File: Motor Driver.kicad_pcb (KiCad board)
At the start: 2 copper layers, 42 parts, among them CON1 AVR-ISP-6, J1 Conn_01x02, J10 Conn_01x04, J3 Conn_01x06, J5 Conn_01x04, J7 Conn_01x02, J8 Conn_01x02, J9 Conn_01x03, Q1 IRF3205, Q2 IRF3205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

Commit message: Minor Changes
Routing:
- net Net-(R5-Pad2): track 5.14 -> 5.92 mm
- net /IN2: track 65.6 -> 66.3 mm
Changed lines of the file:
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@@
     (thickness 1.6)
     (drawings 0)
-    (tracks 348)
+    (tracks 346)
     (zones 0)
     (modules 42)
@@
   (segment (start 133.477 130.135) (end 136.946 130.135) (width 0.6) (layer B.Cu) (net 2))
   (segment (start 136.946 130.135) (end 136.9695 130.1115) (width 0.6) (layer B.Cu) (net 2))
+  (segment (start 79.547318 94.214528) (end 79.547318 92.941736) (width 2) (layer B.Cu) (net 3))
+  (segment (start 79.547318 92.941736) (end 79.5655 92.923554) (width 2) (layer B.Cu) (net 3))
+  (segment (start 79.5655 92.923554) (end 79.5655 91.5035) (width 2) (layer B.Cu) (net 3))
+  (segment (start 94.361 88.773) (end 101.75494 96.16694) (width 2) (layer B.Cu) (net 3))
+  (segment (start 79.5655 91.5035) (end 82.296 88.773) (width 2) (layer B.Cu) (net 3))
+  (segment (start 82.296 88.773) (end 94.361 88.773) (width 2) (layer B.Cu) (net 3))
+  (segment (start 101.75494 96.16694) (end 101.75494 102.4636) (width 2) (layer B.Cu) (net 3))
   (segment (start 107.11688 151.257) (end 107.11688 152.00757) (width 2) (layer B.Cu) (net 3))
   (segment (start 107.11688 152.00757) (end 104.11739 155.00706) (width 2) (layer B.Cu) (net 3))
@@
   (via (at 104.894742 132.490462) (size 1.8) (drill 0.8) (layers F.Cu B.Cu) (net 3))
   (segment (start 107.609 140.421937) (end 106.938063 139.751) (width 2) (layer B.Cu) (net 3))
-  (segment (start 79.547318 94.214528) (end 79.547318 92.941736) (width 2) (layer B.Cu) (net 3))
-  (segment (start 79.547318 92.941736) (end 79.5655 92.923554) (width 2) (layer B.Cu) (net 3))
-  (segment (start 79.5655 92.923554) (end 79.5655 91.5035) (width 2) (layer B.Cu) (net 3))
-  (segment (start 79.5655 91.5035) (end 82.296 88.773) (width 2) (layer B.Cu) (net 3))
-  (segment (start 101.75494 98.71354) (end 101.75494 102.4636) (width 2) (layer B.Cu) (net 3))
-  (segment (start 82.296 88.773) (end 94.361 88.773) (width 2) (layer B.Cu) (net 3))
-  (segment (start 94.361 88.773) (end 95.9485 90.3605) (width 2) (layer B.Cu) (net 3))
-  (segment (start 95.9485 90.3605) (end 95.9485 92.9071) (width 2) (layer B.Cu) (net 3))
-  (segment (start 95.9485 92.9071) (end 101.75494 98.71354) (width 2) (layer B.Cu) (net 3))
   (via (at 94.234 132.461) (size 1.8) (drill 0.8) (layers F.Cu B.Cu) (net 3))
   (segment (start 88.011 132.461) (end 94.234 132.461) (width 0.6) (layer B.Cu) (net 3))
@@
   (segment (start 79.502 143.796) (end 79.502 140.083001) (width 0.6) (layer B.Cu) (net 5))
   (segment (start 79.502 140.083001) (end 79.582 140.003001) (width 0.6) (layer B.Cu) (net 5))
-  (segment (start 85.516318 107.422528) (end 78.702818 107.422528) (width 0.6) (layer B.Cu) (net 6))
-  (segment (start 78.702818 107.422528) (end 76.454 109.671346) (width 0.6) (layer B.Cu) (net 6))
-  (segment (start 76.454 109.671346) (end 76.454 112.75071) (width 0.6) (layer B.Cu) (net 6))
-  (segment (start 76.454 112.75071) (end 76.586818 112.883528) (width 0.6) (layer B.Cu) (net 6))
-  (segment (start 76.586818 112.883528) (end 78.086818 112.883528) (width 0.6) (layer B.Cu) (net 6))
-  (segment (start 77.510531 112.307241) (end 78.086818 112.883528) (width 0.6) (layer B.Cu) (net 6))
+  (segment (start 85.516318 107.422528) (end 77.980629 107.422528) (width 0.6) (layer B.Cu) (net 6))
+  (segment (start 77.980629 107.422528) (end 75.699332 109.703825) (width 0.6) (layer B.Cu) (net 6))
+  (segment (start 75.699332 109.703825) (end 75.699332 112.222694) (width 0.6) (layer B.Cu) (net 6))
+  (segment (start 75.699332 112.222694) (end 76.360166 112.883528) (width 0.6) (layer B.Cu) (net 6))
+  (segment (start 76.360166 112.883528) (end 78.086818 112.883528) (width 0.6) (layer B.Cu) (net 6))
   (segment (start 81.647318 112.892527) (end 78.095817 112.892527) (width 0.6) (layer B.Cu) (net 6))
   (segment (start 78.095817 112.892527) (end 78.086818 112.883528) (width 0.6) (layer B.Cu) (net 6))
+  (segment (start 84.754318 98.151528) (end 84.754318 99.880295) (width 0.6) (layer B.Cu) (net 7))
+  (segment (start 84.754318 99.880295) (end 88.714948 103.840925) (width 0.6) (layer B.Cu) (net 7))
+  (segment (start 88.714948 103.840925) (end 88.714948 107.731748) (width 0.6) (layer B.Cu) (net 7))
+  (segment (start 88.714948 107.731748) (end 87.024168 109.422528) (width 0.6) (layer B.Cu) (net 7))
+  (segment (start 87.024168 109.422528) (end 85.516318 109.422528) (width 0.6) (layer B.Cu) (net 7))
   (segment (start 82.087318 94.214528) (end 82.087318 93.178339) (width 2) (layer B.Cu) (net 7))
   (segment (start 82.087318 93.178339) (end 83.710356 91.555301) (width 2) (layer B.Cu) (net 7))
@@
   (segment (start 89.274768 91.555301) (end 90.215318 92.495851) (width 2) (layer B.Cu) (net 7))
   (segment (start 90.215318 92.495851) (end 90.215318 94.214528) (width 2) (layer B.Cu) (net 7))
-  (segment (start 84.754318 98.151528) (end 84.754318 100.382752) (width 0.6) (layer B.Cu) (net 7))
-  (segment (start 84.754318 100.382752) (end 88.30904 103.937474) (width 0.6) (layer B.Cu) (net 7))
-  (segment (start 88.30904 103.937474) (end 88.30904 108.137656) (width 0.6) (layer B.Cu) (net 7))
-  (segment (start 88.30904 108.137656) (end 87.024168 109.422528) (width 0.6) (layer B.Cu) (net 7))
-  (segment (start 87.024168 109.422528) (end 85.516318 109.422528) (width 0.6) (layer B.Cu) (net 7))
   (segment (start 58.801 122.61088) (end 59.55157 122.61088) (width 2) (layer B.Cu) (net 7))
   (segment (start 59.55157 122.61088) (end 76.839701 105.322749) (width 2) (layer B.Cu) (net 7))
@@
   (segment (start 86.786318 123.932528) (end 86.786318 120.571527) (width 0.6) (layer B.Cu) (net 26))
   (segment (start 86.786318 120.571527) (end 86.727318 120.512527) (width 0.6) (layer B.Cu) (net 26))
-  (segment (start 82.122 140.003001) (end 82.122 141.304) (width 0.6) (layer B.Cu) (net 27))
-  (segment (start 82.122 141.304) (end 84.836 144.018) (width 0.6) (layer B.Cu) (net 27))
+  (segment (start 82.122 140.003001) (end 82.122 142.632228) (width 0.6) (layer B.Cu) (net 27))
+  (segment (start 82.122 142.632228) (end 83.507772 144.018) (width 0.6) (layer B.Cu) (net 27))
+  (segment (start 83.507772 144.018) (end 84.836 144.018) (width 0.6) (layer B.Cu) (net 27))
   (segment (start 74.803 142.875) (end 74.803 142.242001) (width 0.6) (layer B.Cu) (net 28))
   (segment (start 74.803 142.242001) (end 77.042 140.003001) (width 0.6) (layer B.Cu) (net 28))
@@
   (segment (start 136.9695 137.7315) (end 127.34653 137.7315) (width 0.6) (layer B.Cu) (net 39))
   (via (at 120.442939 146.670083) (size 1.8) (drill 0.8) (layers F.Cu B.Cu) (net 39))
+  (segment (start 82.122 132.383001) (end 82.122 133.833948) (width 0.6) (layer B.Cu) (net 41))
+  (segment (start 82.122 133.833948) (end 82.905067 134.617015) (width 0.6) (layer B.Cu) (net 41))
+  (segment (start 96.333341 138.28588) (end 96.333341 144.463712) (width 0.6) (layer B.Cu) (net 41))
+  (segment (start 82.905067 134.617015) (end 92.664476 134.617015) (width 0.6) (layer B.Cu) (net 41))
+  (segment (start 92.664476 134.617015) (end 96.333341 138.28588) (width 0.6) (layer B.Cu) (net 41))
+  (segment (start 96.333341 144.463712) (end 96.333343 144.463714) (width 0.6) (layer B.Cu) (net 41))
   (segment (start 123.549307 143.80441) (end 122.649308 144.704409) (width 0.6) (layer B.Cu) (net 41))
   (segment (start 127.082217 140.2715) (end 123.549307 143.80441) (width 0.6) (layer B.Cu) (net 41))
@@
   (segment (start 96.333343 144.463714) (end 122.408613 144.463714) (width 0.6) (layer F.Cu) (net 41))
   (via (at 122.649308 144.704409) (size 1.8) (drill 0.8) (layers F.Cu B.Cu) (net 41))
-  (segment (start 82.122 132.383001) (end 82.122 132.783001) (width 0.6) (layer B.Cu) (net 41))
-  (segment (start 82.122 132.783001) (end 83.522 134.183001) (width 0.6) (layer B.Cu) (net 41))
-  (segment (start 96.333341 144.463712) (end 96.333343 144.463714) (width 0.6) (layer B.Cu) (net 41))
-  (segment (start 83.522 134.183001) (end 92.230462 134.183001) (width 0.6) (layer B.Cu) (net 41))
-  (segment (start 96.333341 138.28588) (end 96.333341 144.463712) (width 0.6) (layer B.Cu) (net 41))
-  (segment (start 92.230462 134.183001) (end 96.333341 138.28588) (width 0.6) (layer B.Cu) (net 41))
   (via (at 96.333343 144.463714) (size 1.8) (drill 0.8) (layers F.Cu B.Cu) (net 41))
   (segment (start 129.667 143.129) (end 126.873 143.129) (width 0.6) (layer B.Cu) (net 43))

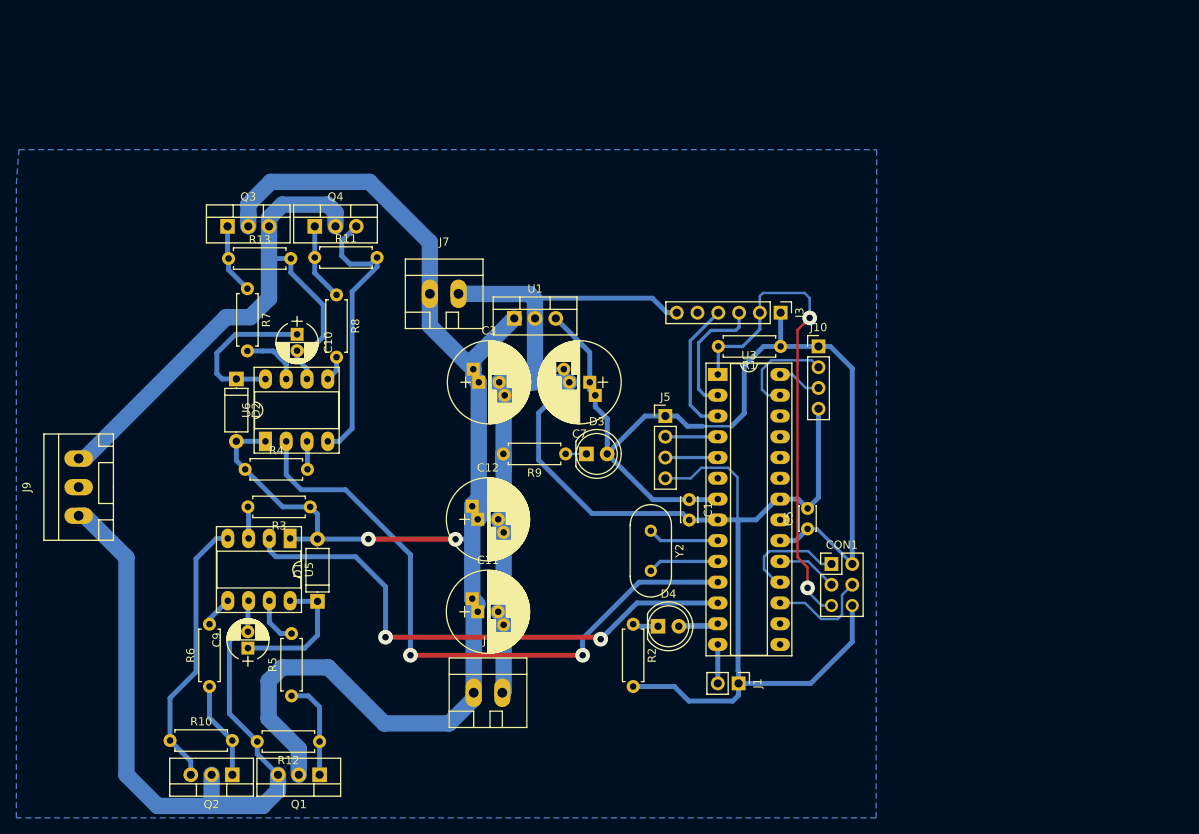
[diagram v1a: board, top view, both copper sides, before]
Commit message: Updated SCH|PCB
Updated the SCh for polarity change on the fly using the 2x2 pinheader
PCB was completely newly designed
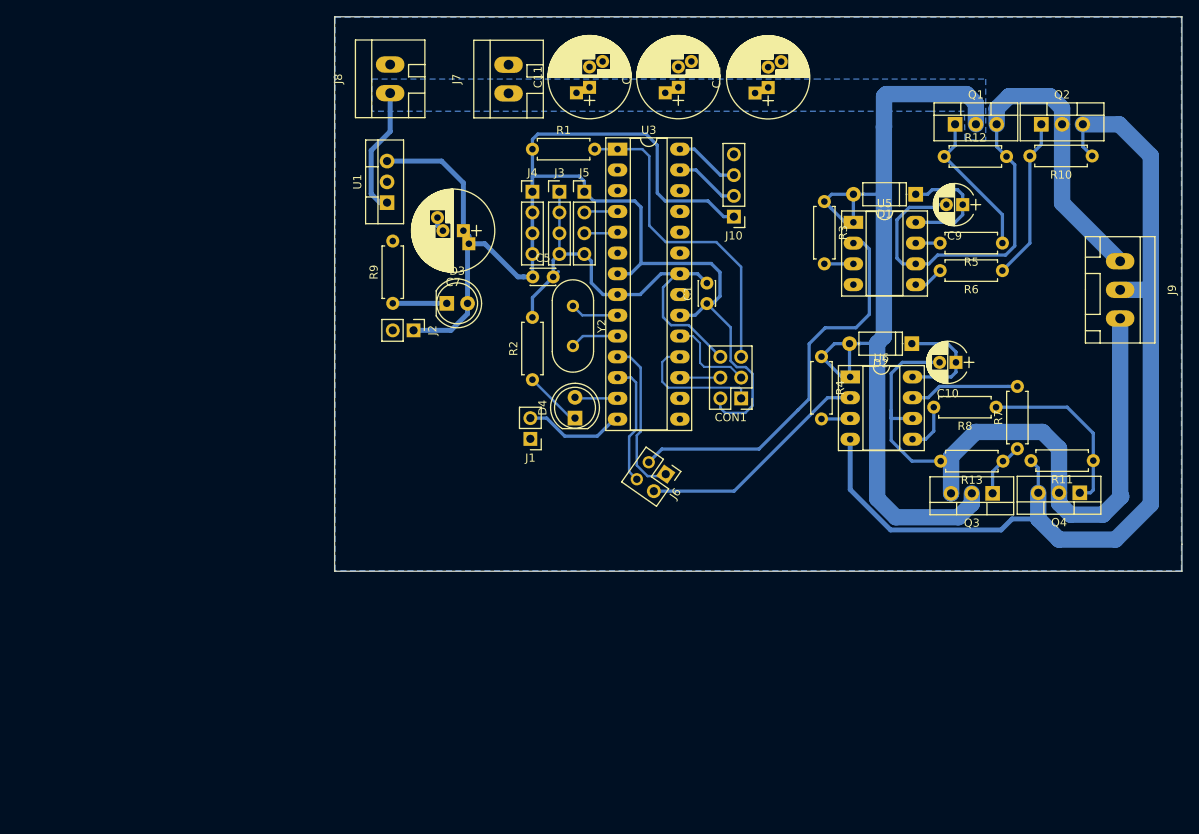
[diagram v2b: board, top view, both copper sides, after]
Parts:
- added J2: Conn_01x02, Pin_Headers:Pin_Header_Straight_1x02_Pitch2.54mm, F.Cu at (99.8, 106.9)
- added J4: Conn_01x04, Pin_Headers:Pin_Header_Straight_1x04_Pitch2.54mm, F.Cu at (114.3, 90.0)
- added J6: Conn_02x02_Odd_Even, Pin_Headers:Pin_Header_Straight_2x02_Pitch2.54mm, F.Cu at (130.6, 124.5)
- J3: value Conn_01x06 -> Conn_01x04; footprint Pin_Headers:Pin_Header_Straight_1x06_Pitch2.54mm -> Pin_Headers:Pin_Header_Straight_1x04_Pitch2.54mm
- moved R10 133.5 mm to (182.8, 85.6), turned to 180 degrees
- moved J9 129.6 mm to (186.2, 102.0), turned to 270 degrees
- moved Q2 127.0 mm to (176.5, 81.7), turned to 0 degrees
- moved Q1 111.2 mm to (166.0, 81.7), turned to 0 degrees
- moved R6 109.5 mm to (171.8, 99.6), turned to 180 degrees
- moved R12 104.7 mm to (164.7, 85.7), turned to 0 degrees
- moved R5 103.1 mm to (171.8, 96.3), turned to 180 degrees
- moved C9 102.9 mm to (166.9, 91.6), turned to 180 degrees
- moved Q3 99.1 mm to (170.6, 126.9), turned to 180 degrees
- moved Q4 99.1 mm to (181.2, 126.8), turned to 180 degrees
- moved R11 98.4 mm to (182.9, 122.9), turned to 180 degrees
- moved R13 97.9 mm to (171.8, 122.9), turned to 180 degrees
- moved R7 96.2 mm to (173.6, 121.4), turned to 90 degrees
- moved D1 88.5 mm to (161.2, 90.3), turned to 180 degrees
- moved D2 82.7 mm to (160.7, 108.6), turned to 180 degrees
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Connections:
- J3 pad 1: +5V -> GND
- J3 pad 2: /RST -> GND
- J3 pad 3: Net-(J3-Pad3) -> GND
- J3 pad 4: Net-(J3-Pad4) -> GND
- U3 pad 2: Net-(J3-Pad3) -> Net-(U3-Pad2)
- U3 pad 3: Net-(J3-Pad4) -> Net-(U3-Pad3)
- U5 pad 2: /IN2 -> Net-(J6-Pad3)
- U6 pad 2: /IN1 -> Net-(J6-Pad2)
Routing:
- net GND: track 308.5 -> 174.6 mm
- net VCC: track 191.3 -> 126.0 mm, vias 2 -> 0
- net /IN1: track 78.1 -> 19.7 mm, vias 2 -> 0
- net +5V: track 115.3 -> 169.9 mm
- net /IN2: track 66.3 -> 15.1 mm, vias 2 -> 0
- net Net-(J6-Pad3): track 0.00 -> 48.6 mm
- net Net-(J6-Pad2): track 0.00 -> 28.8 mm
- net /RST: track 60.6 -> 39.8 mm, vias 2 -> 0
- net Net-(C9-Pad2): track 92.8 -> 75.7 mm
- net Net-(J3-Pad4): track 16.6 -> 0.00 mm
- net Net-(J3-Pad3): track 15.8 -> 0.00 mm
- net Net-(C10-Pad2): track 73.9 -> 87.3 mm
- net Net-(Q4-Pad1): track 9.49 -> 21.9 mm
- net Net-(Q2-Pad1): track 12.0 -> 19.9 mm
- net Net-(CON1-Pad4): track 12.8 -> 4.95 mm
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- added copper zone on B.Cu, net VCC
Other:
- board outline added: 103.6 x 67.8 mm
- net class Default: clearance 0.3 -> 0.254; trace_width 0.3 -> 0.4
- net class Global GND removed
- net class PWR_LOWVoltage removed
- rule pad_to_mask_clearance: 0.2 -> 0
- rule trace_clearance: 0.3 -> 0.254
- rule trace_min: 0.25 -> 0.254
- rule via_min_size: 1.8 -> 1.6
